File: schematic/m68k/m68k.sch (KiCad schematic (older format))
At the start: 45 parts, among them J1 CONN_02X03, J2 CONN_01X03, J3 JTAG, J4 CONN_02X30, J5 I2C, J6 CONN_02X30, J7 CONN_01X02, J8 CONN_02X30, J9 CONN_01X03, SW1 SW_Push_Dual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

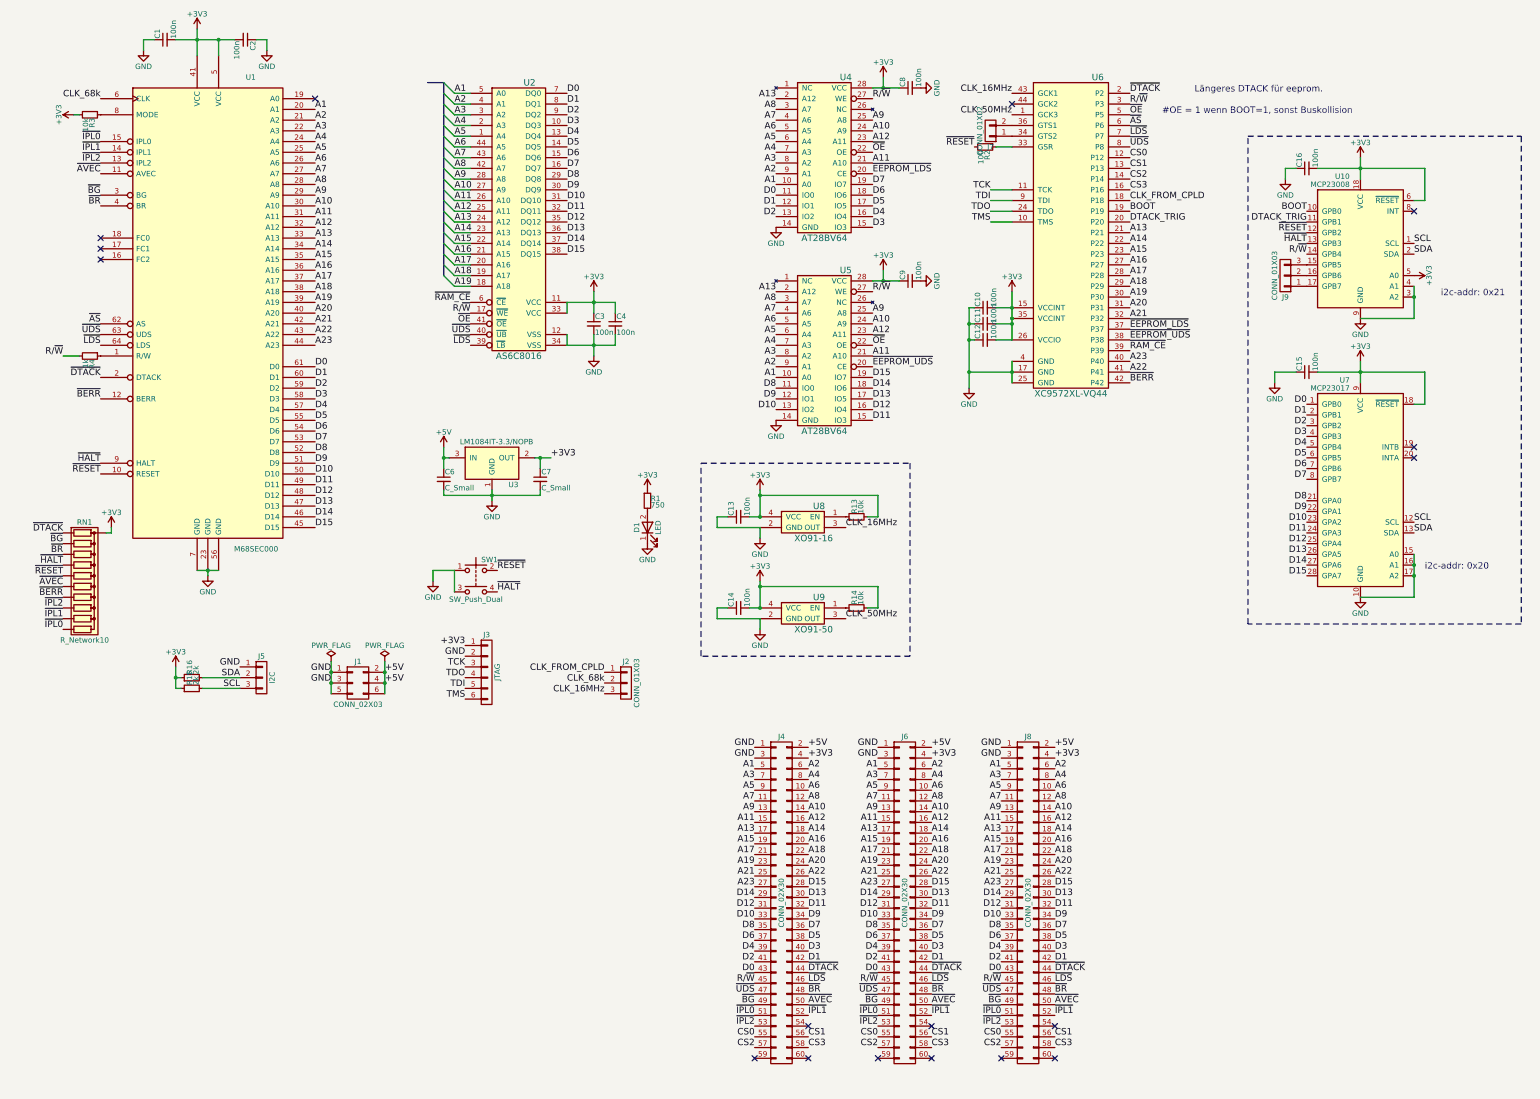
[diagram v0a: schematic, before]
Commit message: - iack fehlt auf m68k - extboard mit dspic30f6014a - zusätzlich propeller für terminal
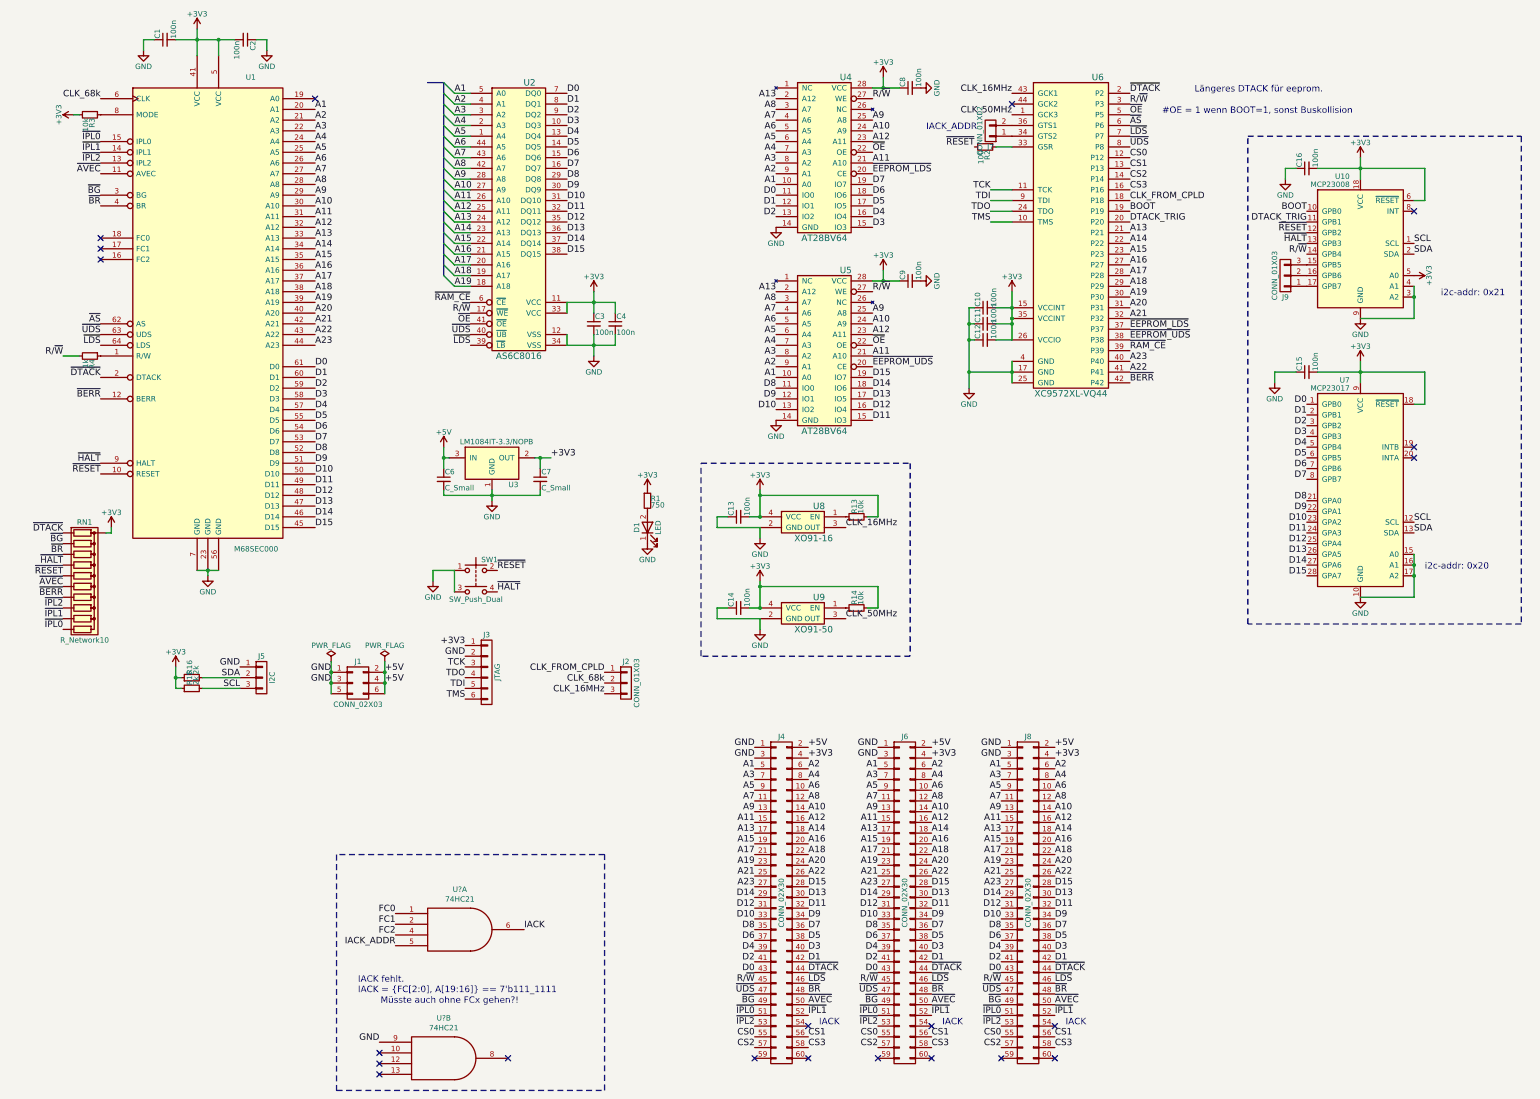
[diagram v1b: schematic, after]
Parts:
- added U? (x2): 74HC21, symbol 74LS21
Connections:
- net GND: now also U?.7 (GND), U?.7 (GND), U?.9
- new net FC0: U?.1
- new net FC1: U?.2
- new net FC2: U?.4
- new net IACK: U?.6
- new net IACK_ADDR: U?.5
- new net VCC: U?.14 (VCC), U?.14 (VCC)
- no-connect marks 17 -> 21
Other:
- note added: "IACK"
- note added: "IACK fehlt.\nIACK = {FC[2:0], A[19:16]} == 7'b111_1111"
- note added: "IACK_ADDR"
- note added: "Müsste auch ohne FCx gehen?!"
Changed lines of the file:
@@
 LIBS:custom
 LIBS:switches
-EELAYER 25 0
+LIBS:m68k-cache
+EELAYER 26 0
 EELAYER END
 $Descr A3 16535 11693
@@
 Connection ~ 3400 6750
 Connection ~ 3900 6750
+Text Notes 3650 9750 0    60   ~ 0
+IACK fehlt.\nIACK = {FC[2:0], A[19:16]} == 7'b111_1111
+Text Notes 7950 10050 0    60   ~ 0
+IACK
+Text Notes 9100 10050 0    60   ~ 0
+IACK
+Text Notes 10250 10050 0    60   ~ 0
+IACK
+Text Notes 8950 1700 0    60   ~ 0
+IACK_ADDR
+$Comp
+L 74LS21 U?
+U 1 1 59BA6149
+P 4600 9150
+F 0 "U?" H 4600 9525 50  0000 C CNN
+F 1 "74HC21" H 4600 9434 50  0000 C CNN
+F 2 "" H 4600 9150 50  0001 C CNN
+F 3 "" H 4600 9150 50  0001 C CNN
+	1    4600 9150
+	1    0    0    -1
+$EndComp
+Text Label 5200 9150 0    60   ~ 0
+IACK
+Text Label 4000 9000 2    60   ~ 0
+FC0
+Text Label 4000 9100 2    60   ~ 0
+FC1
+Text Label 4000 9200 2    60   ~ 0
+FC2
+Text Label 4000 9300 2    60   ~ 0
+IACK_ADDR
+$Comp
+L 74LS21 U?
+U 2 1 59BA7BD3
+P 4450 10350
+F 0 "U?" H 4450 10725 50  0000 C CNN
+F 1 "74HC21" H 4450 10634 50  0000 C CNN
+F 2 "" H 4450 10350 50  0001 C CNN
+F 3 "" H 4450 10350 50  0001 C CNN
+	2    4450 10350
+	1    0    0    -1
+$EndComp
+Text Label 3850 10200 2    60   ~ 0
+GND
+NoConn ~ 3850 10300
+NoConn ~ 3850 10400
+NoConn ~ 3850 10500
+NoConn ~ 5050 10350
+Text Notes 5150 9850 2    60   ~ 0
+Müsste auch ohne FCx gehen?!
+Wire Notes Line
+	3450 8450 3450 10650
+Wire Notes Line
+	3450 10650 5950 10650
+Wire Notes Line
+	5950 10650 5950 8450
+Wire Notes Line
+	5950 8450 3450 8450
 $EndSCHEMATC
